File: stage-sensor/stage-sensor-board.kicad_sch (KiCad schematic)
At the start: 11 parts, among them J1 STEMMA QT, U1 ICM 42605, U3 SHT45

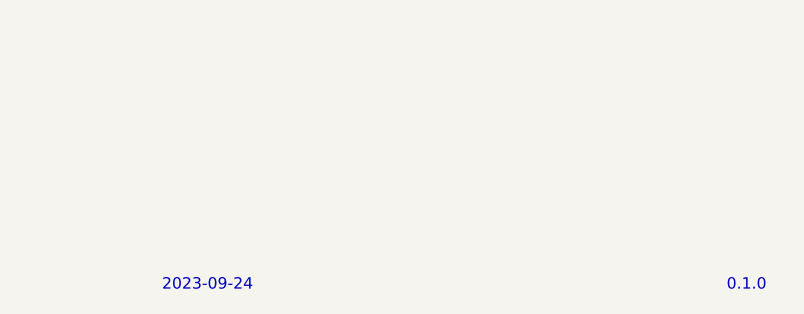
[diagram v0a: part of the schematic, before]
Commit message: Stage sensor board V0.1.1
Switched out the vertical stemma QT for horizontal one. Funciontally equivalent to V0.1.1 WIll send this one over for production.
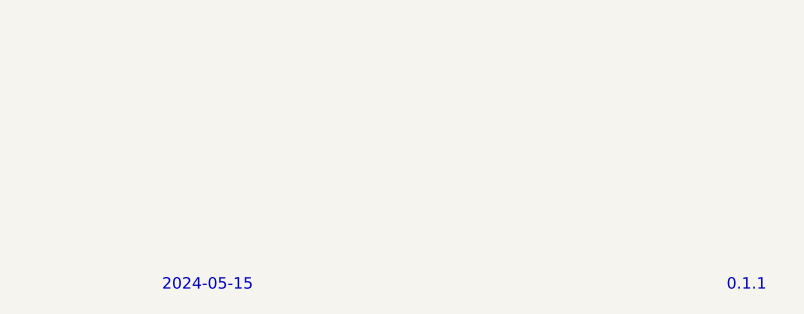
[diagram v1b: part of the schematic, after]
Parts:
- J1: footprint Connector_JST:JST_SH_BM04B-SRSS-TB_1x04-1MP_P1.00mm_Vertical -> Connector_JST:JST_SH_SM04B-SRSS-TB_1x04-1MP_P1.00mm_Horizontal; Mouser (none) -> 306-SM04BSRSSTBLFDNP
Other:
- note added: "0.1.1"
- note added: "2024-05-15"
- note removed: "0.1.0"
- note removed: "2023-09-24"
